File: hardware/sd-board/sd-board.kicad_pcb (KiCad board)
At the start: 2 copper layers, 22.4 x 41.5 mm, 9 parts, among them J1 TF-01A push-push, J2 FFC 6P 0.5mm, U1 74LVC1G04

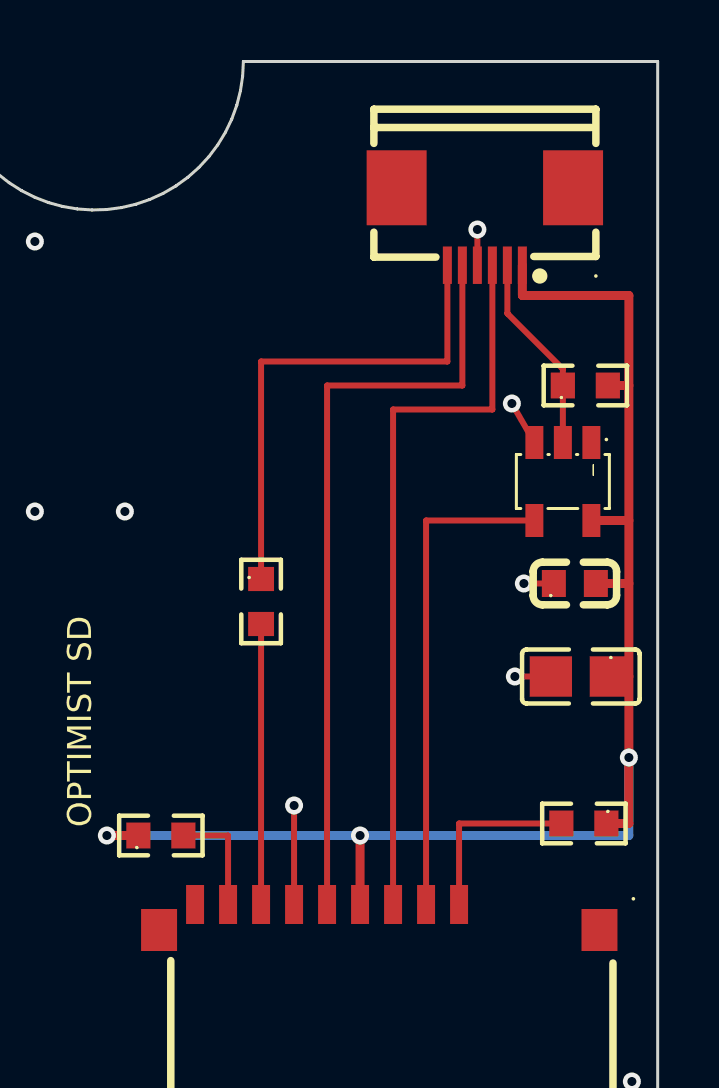
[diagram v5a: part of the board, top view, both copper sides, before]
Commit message: feat(hardware): the FFC socket's cable side 5 mm under the board's top (35 mm up, 9 under the speaker plug; the user), the lines and U1's group 3.5 mm lower, R2 at 14; DRC 0, nets 0 differ
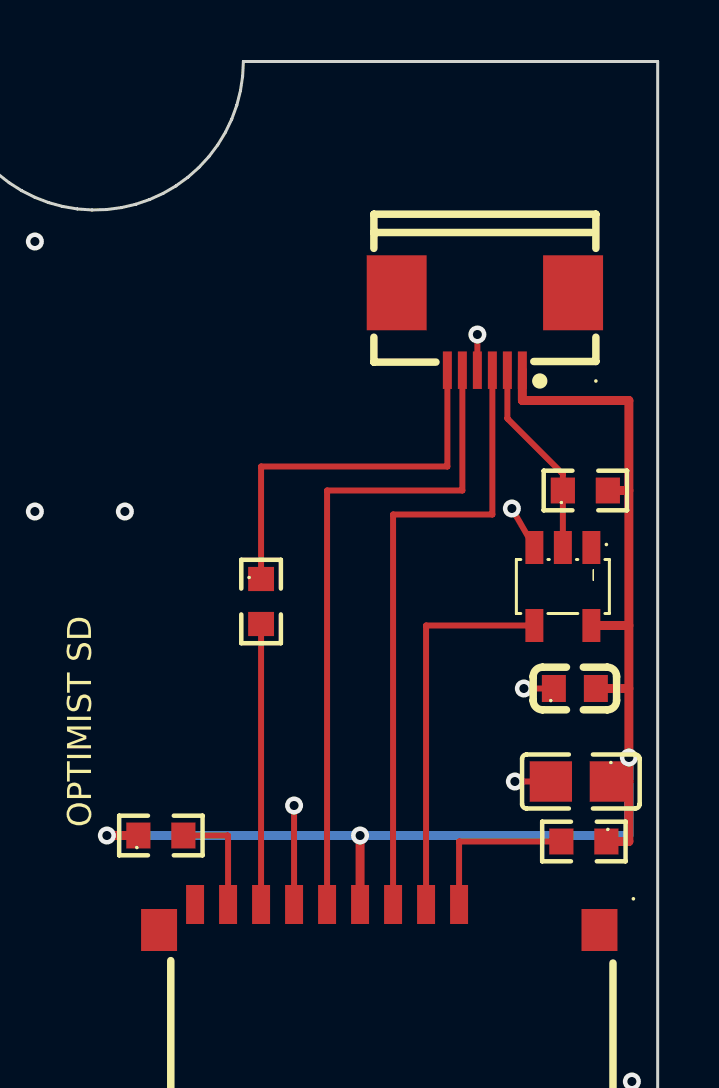
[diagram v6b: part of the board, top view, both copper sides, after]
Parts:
- moved C1 3.50 mm to (194.2, 184.0)
- moved C2 3.50 mm to (194.0, 180.9)
- moved J2 3.50 mm to (191.0, 169.0)
- moved R4 3.50 mm to (194.3, 174.3)
- moved U1 3.50 mm to (193.6, 177.5)
- moved R2 0.60 mm to (194.3, 186.0)
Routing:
- net MOSI: track 24.6 -> 21.1 mm
- net MISO: track 16.7 -> 13.2 mm
- net CLK: track 25.8 -> 22.3 mm
- net CARD_CS: track 16.4 -> 12.9 mm
- net 3V3: track 49.9 -> 47.0 mm
- net DAT2: track 6.11 -> 5.51 mm

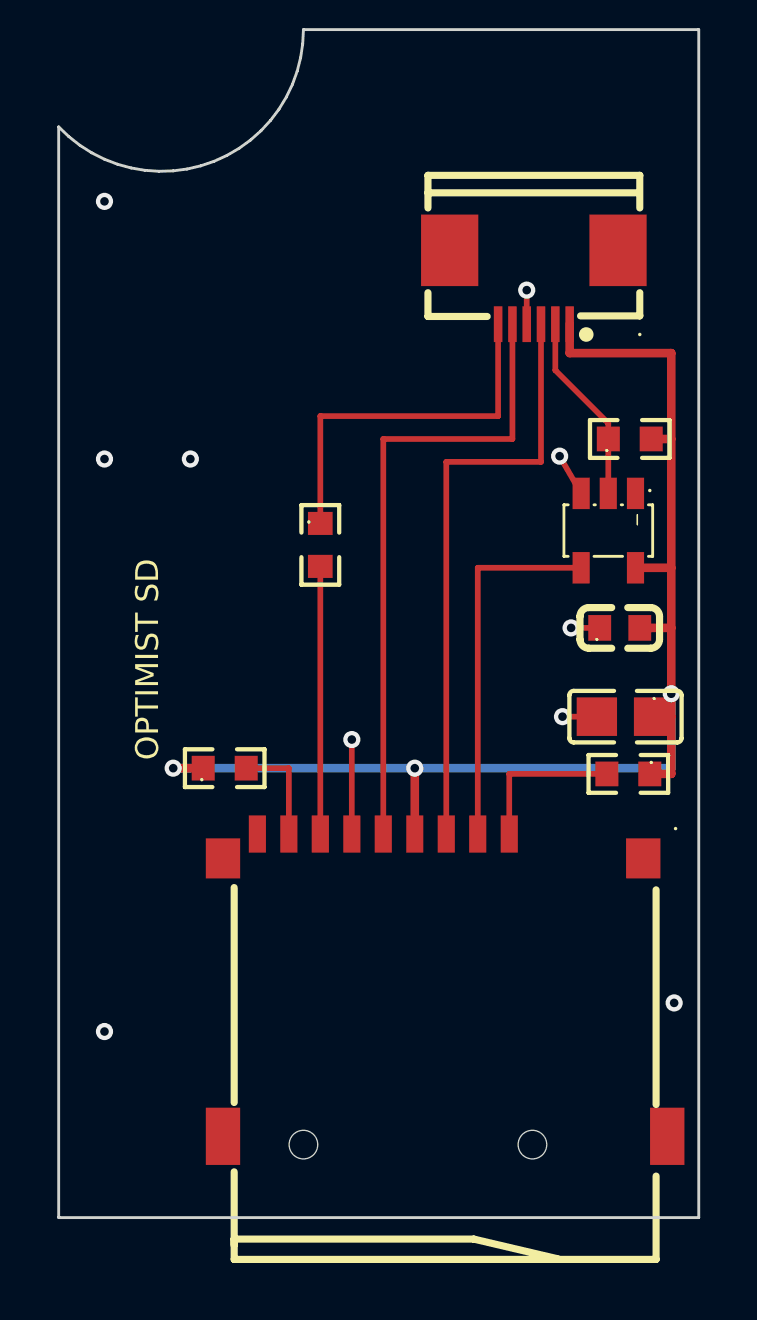
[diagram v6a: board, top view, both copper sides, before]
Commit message: feat(hardware): the card socket in the board's middle (the user; the card 81.7 mm from the left wall), the FFC socket's cable side 10 mm under the board's top, U1's group lower, C1 to the left; DRC 0, nets 0 differ
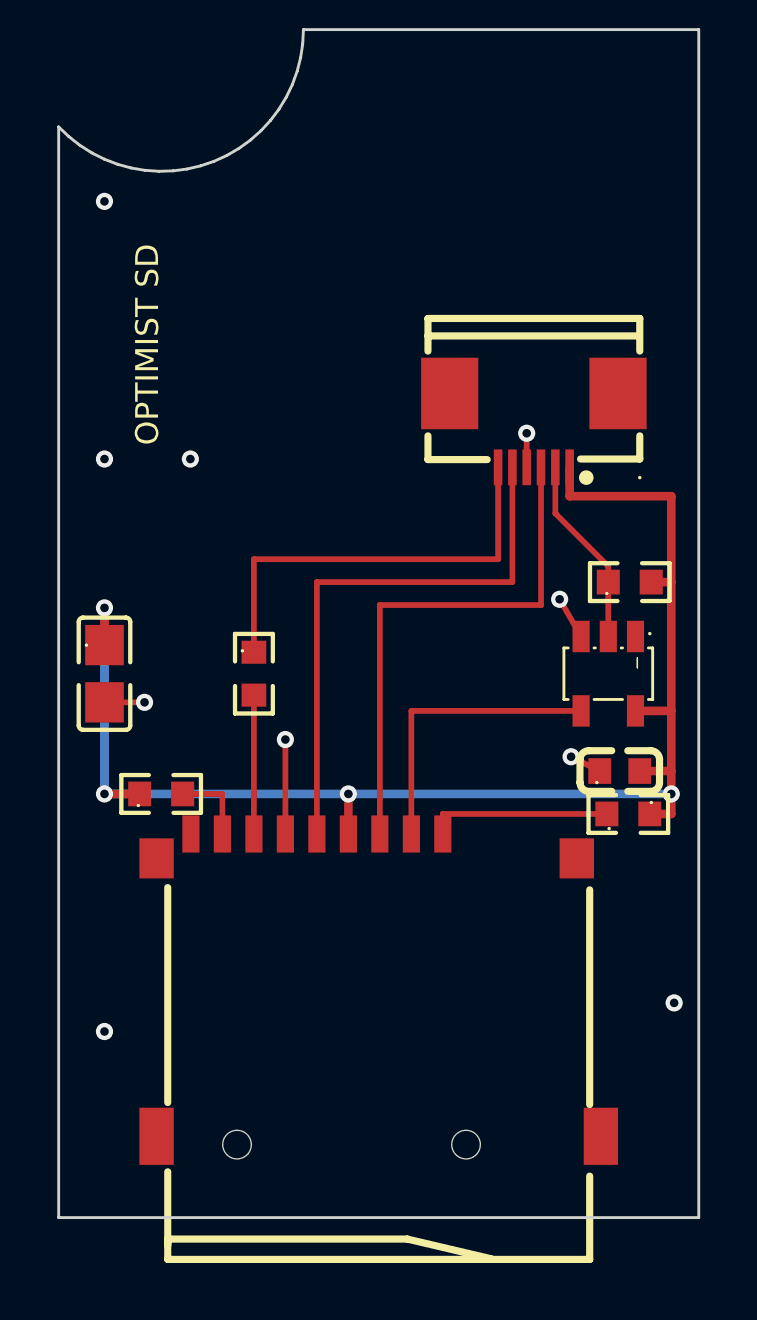
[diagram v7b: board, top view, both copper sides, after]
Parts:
- moved C1 18.3 mm to (176.0, 182.5), turned to -90 degrees
- moved R1 5.06 mm to (181.2, 182.5)
- moved C2 5.00 mm to (194.0, 185.9)
- moved J2 5.00 mm to (191.0, 174.0)
- moved R4 5.00 mm to (194.3, 179.3)
- moved U1 5.00 mm to (193.6, 182.5)
- moved R3 2.40 mm to (178.0, 186.7)
- moved J1 2.32 mm to (185.6, 193.4)
- moved R2 1.40 mm to (194.3, 187.4)
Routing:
- net DAT0: track 9.35 -> 4.85 mm
- net MOSI: track 21.1 -> 18.4 mm
- net CARD_CS: track 12.9 -> 10.2 mm
- net 3V3: track 47.0 -> 49.7 mm, vias 3 -> 4
- net CLK: track 22.3 -> 19.6 mm
- net MISO: track 13.2 -> 15.0 mm
- net DAT1: track 3.79 -> 2.79 mm
- net DAT2: track 5.51 -> 6.43 mm

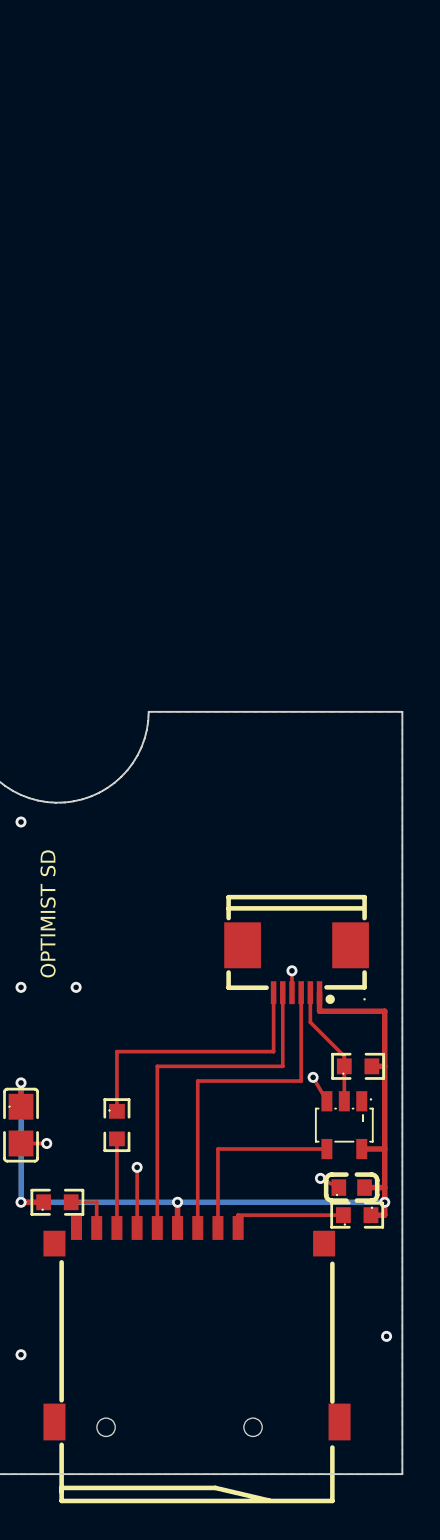
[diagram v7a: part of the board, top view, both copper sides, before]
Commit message: feat(hardware): SD board v5, the board is also the splitter (the user): two 10-pin 0.5 mm sockets (HCTL HC-FPC-05-09-10RLTAG, C5213750: JLCPCB stock and SMT assembly, contacts on both sides, 1 mm tall), J3 for the LCD's own cable against the jacks, J2 for a cable from J12 below it, all 10 lines through; a column up the right of the speaker plug to a head under the jacks; the tray stays under the lower part. The J12 pin order is a PROVISIONAL guess (LCD_PINS): not to be ordered before the pin map; DRC 0, nets 0 differ
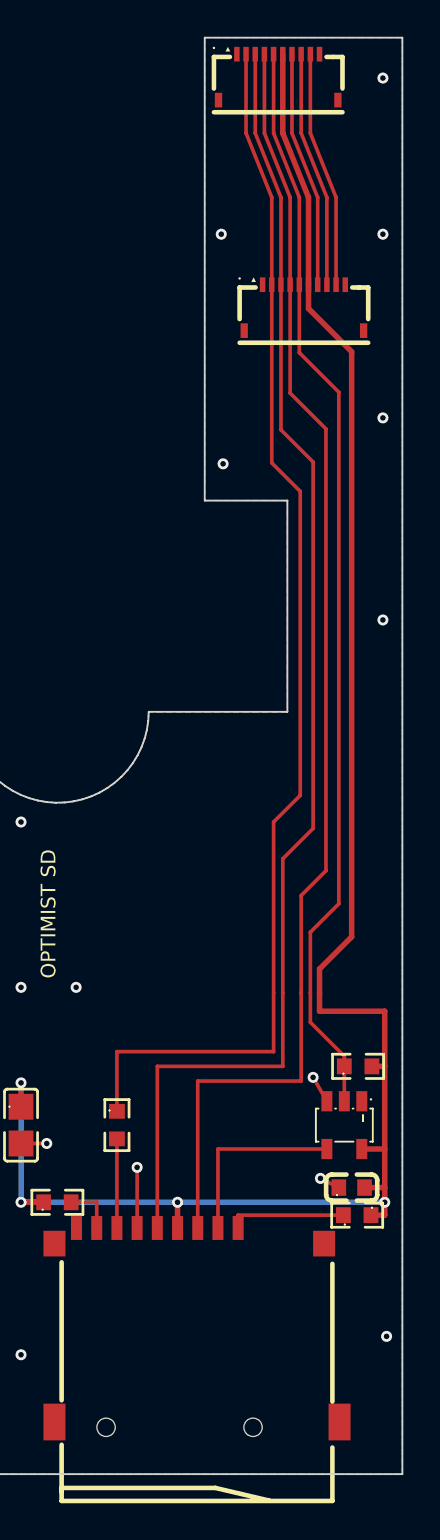
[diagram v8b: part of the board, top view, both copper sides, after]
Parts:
- added J3: FPC 10P 0.5mm (LCD), sdboard:FPC-SMD_10P-P0.50_HC-FPC-05-09-10RLTAG, F.Cu at (190.0, 125.5)
- J2: value FFC 6P 0.5mm -> FPC 10P 0.5mm (IN); footprint sdboard:FPC-SMD_6P-P0.50_XUNPU_FPC-05F-6PH20 -> sdboard:FPC-SMD_10P-P0.50_HC-FPC-05-09-10RLTAG
- moved J2 36.0 mm to (191.4, 138.0)
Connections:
- J2 pad 1: 3V3 -> GND
- J2 pad 2: LCD_CS -> MISO
- J2 pad 3: MOSI -> CLK
- J2 pad 4: GND -> MOSI
- J2 pad 5: CLK -> LCD_CS
- J2 pad 6: MISO -> 3V3
- J2 pad 7: GND -> LCD_RST
- J2 pad 8: GND -> LCD_LEDA
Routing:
- net 3V3: track 49.7 -> 102.7 mm
- net LCD_CS: track 6.68 -> 59.6 mm
- net CLK: track 19.6 -> 72.4 mm
- net MOSI: track 18.4 -> 71.2 mm
- net MISO: track 15.0 -> 67.6 mm
- net LCD_RST: track 0.00 -> 12.8 mm
- net LCD_LEDK: track 0.00 -> 12.8 mm
- net LCD_LEDA: track 0.00 -> 12.8 mm
- net GND: track 8.51 -> 7.32 mm, vias 10 -> 15
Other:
- board size 22.4 x 41.5 mm -> 22.4 x 78.2 mm
